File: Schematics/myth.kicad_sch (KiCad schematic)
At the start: 137 parts, among them J1 Conn_01x08_Male, J10 Conn_01x04_Male, J11 Conn_02x01, J2 Conn_01x08_Male, J3 Conn_01x08_Male, J4 Conn_01x08_Male, J5 Conn_01x08_Male, J6 Conn_01x08_Male, J8 Conn_01x08_Male, J9 Conn_01x04_Male, U1 74AHC02, U10 74HC595, U11 74HC165, U12 74AHC08, U13 74HC238, U14 74HC238, U15 74HC238, U16 4002, U17 74HC32, U18 74AHC273, U19 74LS32, U2 74AHC273, U20 CD4532BE, U21 74AHC138, U22 74AHC04, U23 74AHC138, U24 74HC238, U25 74HC238, U26 74LS32, U27 4078, U28 74AHC244, U29 74AHC138, U3 74HC74, U30 74AHC138, U31 4075, U32 74AHC02, U33 74AHC138, U34 74HC238, U35 74AHC138, U36 74HC163, U37 74AHC574, U38 74HC238, U39 74HC32, U4 74AHC04, U40 74AHC04, U41 74AHC574, U42 74HC74, U43 74AHC273, U44 74HC283, U45 74HC283, U46 74AHC273, U47 74HC02, U48 74HC157, U49 74HC157, U5 74AHC04, U50 74AHC244, U51 74AHC04, U52 74HC283, U53 74HC193, U54 74HC193, U55 74HC193, U56 74HC193, U57 74AHC273, U58 74HC193, U59 74HC193, U6 74AHC08, U60 74AHC244, U61 74LS32, U62 4078, U63 74LS08, U64 74LS21, U65 74AHC04, U66 74AHC273, U67 74HC157, U68 74HC157, U7 74HC00, U71 74LS257, U72 74LS257, U73 74HC04, U74 74HC157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

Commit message: Rename G to D as before (D for Data)
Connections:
- net GETG renamed GETD
- net xG renamed xD
- net ~{BOG} renamed ~{BOD}
- net ~{CMacc}: no longer names the net of U47.10, U50.1 (1OE), U50.19 (2OE)
- net ~{COG} renamed ~{COD}
- net ~{GETG} renamed ~{GETD}
- net ~{Gx} renamed ~{Dx}
- net ~{MGacc}: no longer names the net of U47.4, U80.1 (1OE), U80.19 (2OE)
- net ~{MLacc}: no longer names the net of U19.8, U60.1 (1OE), U60.19 (2OE)
- net ~{PUTG} renamed ~{PUTD}
- net ~{opc_GIRO} renamed ~{opc_DIRO}
- net ~{xG} renamed ~{xD}
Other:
- note added: "(DATA) Page Index"
- note added: "D"
- note added: "D/I/R/O"
- note added: "Implementation Semantics: CALL/TRAP: I <= PC, Co <= C, decrement L, PC <= 0, C <= DB0-7 RET: C <= L7, PC <= I, increment L COR: C <= D, PC <= I NEW: L7 <= Co xB does PC-relative in-page branching"
- note removed: "(GLOBAL) Page Index"
- note removed: "G"
- note removed: "G/I/R/O"
- note removed: "Implementation Semantics: CALL/TRAP: I <= PC, Co <= C, decrement L, PC <= 0, C <= DB0-7 RET: C <= L7, PC <= I, increment L COR: C <= G, PC <= I NEW: L7 <= Co xB does a PC-relative in-page branching"
- moved on the sheet: U19C, U32C
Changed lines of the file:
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@@
 	)
 	(junction
+		(at 481.3933 526.1862)
+		(diameter 0)
+		(color 0 0 0 0)
+	)
+	(junction
 		(at 694.4732 536.6399)
 		(diameter 0)
@@
 		)
 	)
+	(wire
+		(pts
+			(xy 484.8212 551.8524) (xy 481.3933 551.8524)
+		)
+		(stroke
+			(width 0)
+			(type default)
+		)
+	)
 	(polyline
 		(pts
@@
 	(wire
 		(pts
-			(xy 533.1407 532.1854) (xy 535.6807 532.1854)
+			(xy 502.6012 554.3924) (xy 500.0612 554.3924)
 		)
 		(stroke
@@
 	(wire
 		(pts
+			(xy 481.3933 551.8524) (xy 481.3933 526.1862)
+		)
+		(stroke
+			(width 0)
+			(type default)
+		)
+	)
+	(wire
+		(pts
 			(xy 1038.9126 182.7303) (xy 1038.9126 221.0698)
 		)
@@
 		)
 	)
-	(text "(GLOBAL)\nPage Index"
+	(text "(DATA)\nPage Index"
 		(exclude_from_sim no)
 		(at 886.2679 522.7559 0)
@@
 		)
 	)
-	(text "G"
+	(text "D"
 		(exclude_from_sim no)
 		(at 870.7275 525.6869 0)
@@
 		)
 	)
-	(text "G/I/R/O"
+	(text "D/I/R/O"
 		(exclude_from_sim no)
 		(at 84.0854 511.9029 0)
@@
 		)
 	)
-	(text "Implementation Semantics:\n\nCALL/TRAP: I <= PC, Co <= C, decrement L, PC <= 0, C <= DB0-7\nRET: C <= L7, PC <= I, increment L\nCOR: C <= G, PC <= I\nNEW: L7 <= Co\n\nxB does a PC-relative in-page branching\n\n"
+	(text "Implementation Semantics:\n\nCALL/TRAP: I <= PC, Co <= C, decrement L, PC <= 0, C <= DB0-7\nRET: C <= L7, PC <= I, increment L\nCOR: C <= D, PC <= I\nNEW: L7 <= Co\n\nxB does PC-relative in-page branching\n\n"
 		(exclude_from_sim no)
 		(at 967.3252 481.683 0)
@@
 	(text "L"
 		(exclude_from_sim no)
-		(at 478.8371 570.0052 0)
+		(at 485.7704 594.8623 0)
 		(effects
 			(font
@@
 	(text "(LOCAL)\nPage index\n(Stack Pointer)"
 		(exclude_from_sim no)
-		(at 494.1251 573.1581 0)
+		(at 501.0584 598.0152 0)
 		(effects
 			(font
@@
 		)
 	)
-	(label "~{CMacc}"
-		(at 694.4732 557.0975 0)
-		(fields_autoplaced yes)
-		(effects
-			(font
-				(size 1.27 1.27)
-			)
-			(justify left bottom)
-		)
-	)
 	(label "FETCH"
 		(at 838.3299 618.4854 180)
@@
 		)
 	)
-	(label "~{GETG}"
+	(label "~{GETD}"
 		(at 746.9641 205.0748 180)
 		(fields_autoplaced yes)
@@
 		)
 	)
-	(label "~{COG}"
+	(label "~{COD}"
 		(at 809.2739 506.3054 180)
 		(fields_autoplaced yes)
@@
 		)
 	)
-	(label "~{MLacc}"
-		(at 550.9207 534.7254 0)
-		(fields_autoplaced yes)
-		(effects
-			(font
-				(size 1.27 1.27)
-			)
-			(justify left bottom)
-		)
-	)
 	(label "PC6"
 		(at 501.9639 208.5014 180)
@@
 		)
 	)
-	(label "~{GETG}"
+	(label "~{GETD}"
 		(at 115.4329 510.5003 0)
 		(fields_autoplaced yes)
@@
 		)
 	)
-	(label "~{opc_GIRO}"
+	(label "~{opc_DIRO}"
 		(at 254.1778 504.1138 0)
 		(fields_autoplaced yes)
@@
 		)
 	)
-	(label "~{BOG}"
+	(label "~{BOD}"
 		(at 834.6739 452.9654 0)
 		(fields_autoplaced yes)
@@
 		)
 	)
-	(label "~{MGacc}"
-		(at 901.9905 417.0084 0)
-		(fields_autoplaced yes)
-		(effects
-			(font
-				(size 1.27 1.27)
-			)
-			(justify left bottom)
-		)
-	)
 	(label "xA"
 		(at 364.9218 304.4698 0)
@@
 		)
 	)
-	(label "GETG"
+	(label "GETD"
 		(at 762.2041 205.0748 0)
 		(fields_autoplaced yes)
@@
 		)
 	)
-	(label "~{Gx}"
+	(label "~{Dx}"
 		(at 362.3818 381.3048 0)
 		(fields_autoplaced yes)
@@
 		)
 	)
-	(label "~{opc_GIRO}"
+	(label "~{opc_DIRO}"
 		(at 67.1729 520.6603 180)
 		(fields_autoplaced yes)
@@
 		)
 	)
-	(label "~{Gx}"
+	(label "~{Dx}"
 		(at 871.5671 479.3249 0)
 		(fields_autoplaced yes)
@@
 		)
 	)
-	(label "~{PUTG}"
+	(label "~{PUTD}"
 		(at 886.8071 481.8649 0)
 		(fields_autoplaced yes)
@@
 		)
 	)
-	(label "~{MLacc}"
-		(at 481.3933 523.6462 180)
-		(fields_autoplaced yes)
-		(effects
-			(font
-				(size 1.27 1.27)
-			)
-			(justify right bottom)
-		)
-	)
 	(label "~{COI}"
 		(at 557.3853 219.1739 180)
@@
 		)
 	)
-	(label "~{COG}"
+	(label "~{COD}"
 		(at 834.6739 447.8854 0)
 		(fields_autoplaced yes)
@@
 		)
 	)
-	(label "~{xG}"
+	(label "~{xD}"
 		(at 706.2737 218.708 180)
 		(fields_autoplaced yes)
@@
 		)
 	)
-	(label "xG"
+	(label "xD"
 		(at 721.5137 218.708 0)
 		(fields_autoplaced yes)
@@
 	)
 	(label "Lx_pre"
-		(at 517.9007 529.6454 180)
+		(at 517.8412 556.9324 0)
 		(fields_autoplaced yes)
 		(effects
@@
 				(size 1.27 1.27)
 			)
-			(justify right bottom)
+			(justify left bottom)
 		)
 	)
@@
 		)
 	)
-	(label "xG"
+	(label "xD"
 		(at 787.454 498.6854 180)
 		(fields_autoplaced yes)
@@
 		)
 	)
-	(label "~{xG}"
+	(label "~{xD}"
 		(at 364.2868 271.4498 0)
 		(fields_autoplaced yes)
@@
 	)
 	(label "GETPUT"
-		(at 535.6807 537.2654 180)
+		(at 500.0612 549.3124 0)
 		(fields_autoplaced yes)
 		(effects
@@
 				(size 1.27 1.27)
 			)
-			(justify right bottom)
+			(justify left bottom)
 		)
 	)
@@
 		)
 	)
-	(label "~{PUTG}"
+	(label "~{PUTD}"
 		(at 115.4329 520.6603 0)
 		(fields_autoplaced yes)
@@
 		)
 	)
-	(label "GETG"
+	(label "GETD"
 		(at 787.454 503.7654 180)
 		(fields_autoplaced yes)
@@
 	)
 	(label "xL_pre"
-		(at 517.9007 534.7254 180)
+		(at 517.8412 551.8524 0)
 		(fields_autoplaced yes)
 		(effects
@@
 				(size 1.27 1.27)
 			)
-			(justify right bottom)
+			(justify left bottom)
 		)
 	)
@@
 		)
 	)
-	(label "~{BOG}"
+	(label "~{BOD}"
 		(at 809.2739 508.8454 180)
 		(fields_autoplaced yes)
@@
 	(symbol
 		(lib_id "74xx:74LS02")
-		(at 525.5207 532.1854 0)
+		(at 510.2212 554.3924 180)
 		(unit 3)
 		(exclude_from_sim no)
@@
 		(dnp no)
 		(property "Reference" "U32"
-			(at 525.5207 523.9304 0)
+			(at 510.2212 562.6474 0)
 			(effects
 				(font
@@
 		)
 		(property "Value" "74AHC02"
-			(at 525.5207 526.2418 0)
+			(at 510.2212 560.336 0)
 			(effects
 				(font
@@
 		)
 		(property "Footprint" "Package_DIP:DIP-14_W7.62mm_Socket_LongPads"
-			(at 525.5207 532.1854 0)
+			(at 510.2212 554.3924 0)
 			(effects
 				(font
@@
 		)
 		(property "Datasheet" "http://www.ti.com/lit/gpn/sn74ls02"
-			(at 525.5207 532.1854 0)
+			(at 510.2212 554.3924 0)
 			(effects
 				(font
@@
 		)
 		(property "Description" ""
-			(at 525.5207 532.1854 0)
+			(at 510.2212 554.3924 0)
 			(effects
 				(font
@@
 	(symbol
 		(lib_id "74xx:74LS32")
-		(at 543.3007 534.7254 0)
+		(at 492.4412 551.8524 180)
 		(unit 3)
 		(exclude_from_sim no)
@@
 		(fields_autoplaced yes)
 		(property "Reference" "U19"
-			(at 543.3007 526.7709 0)
+			(at 492.4412 559.8069 0)
 			(effects
 				(font
@@
 		)
 		(property "Value" "74LS32"
-			(at 543.3007 529.1952 0)
+			(at 492.4412 557.3826 0)
 			(effects
 				(font
@@
 		)
 		(property "Footprint" ""
-			(at 543.3007 534.7254 0)
+			(at 492.4412 551.8524 0)
 			(effects
 				(font
@@
 		)
 		(property "Datasheet" "http://www.ti.com/lit/gpn/sn74LS32"
-			(at 543.3007 534.7254 0)
+			(at 492.4412 551.8524 0)
 			(effects
 				(font
@@
 		)
 		(property "Description" "Quad 2-input OR"
-			(at 543.3007 534.7254 0)
+			(at 492.4412 551.8524 0)
 			(effects
 				(font

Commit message: Relocate pre-built symbol table
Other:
- note added: "NL => NOP (reserved) NM => NOP (reserved) LL => NOP (reserved) LM => NOP (reserved) ML => NOP (reserved) MM => NOP (reserved) DD => NOP (reserved) RR => NOP (reserved) II => NOP (reserved)"
- note added: "Relative Addressing"
- note removed: "NL => NOP (reserved) NM => NOP (reserved) LL => NOP (reserved) LM => NOP (reserved) ML => NOP (reserved) MM => NOP (reserved) GG => NOP (reserved) RR => NOP (reserved) II => NOP (reserved)"
- note removed: "Relative Addressing Unit"
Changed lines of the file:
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@@
 		)
 	)
-	(text "                   NL => NOP (reserved)\n                   NM => NOP (reserved)\n                   LL => NOP (reserved)\n                   LM => NOP (reserved)\n                   ML => NOP (reserved)\n                   MM => NOP (reserved)\n                   GG => NOP (reserved)\n                   RR => NOP (reserved)\n                   II => NOP (reserved)"
+	(text "                   NL => NOP (reserved)\n                   NM => NOP (reserved)\n                   LL => NOP (reserved)\n                   LM => NOP (reserved)\n                   ML => NOP (reserved)\n                   MM => NOP (reserved)\n                   DD => NOP (reserved)\n                   RR => NOP (reserved)\n                   II => NOP (reserved)"
 		(exclude_from_sim no)
 		(at 194.3077 303.7819 0)
 		(effects
 			(font
+				(face "Monaco")
 				(size 1.27 1.27)
 			)
 		)
 	)
-	(text "Relative Addressing Unit"
+	(text "Relative Addressing"
 		(exclude_from_sim no)
-		(at 402.8152 312.0424 0)
+		(at 414.6633 310.4758 0)
 		(effects
 			(font

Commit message: Change mnemonic for NEW to OWN and reorder VM struct
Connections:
- net NEW renamed OWN
- net ~{NEW} renamed ~{OWN}
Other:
- note added: "0 CLR ("Clear" / R:=0) 1 IDO ("Identity O" / R:=O) 2 OCR ("Ones Complement R" / R:=~R) 3 OCO ("Ones Complement O" / R:=~O) 4 SLR ("Shift left R" / R:=R<<1) 5 SLO ("Shift left O" / R:=O<<1) 6 SRR ("Shift right R" / R:=R>>1) 7 SRO ("Shift right O" / R:=O>>1)"
- note added: "Hard wire so that OWN and RET reference L7 ("Owner")"
- note added: "Implementation Semantics: CALL/TRAP: I <= PC, Co <= C, decrement L, PC <= 0, C <= DB0-7 RET: C <= L7, PC <= I, increment L COR: C <= D, PC <= I OWN: L7 <= Co xB does PC-relative in-page branching"
- note removed: "0 CLR ("Clear" / R:=0) 1 IDO ("Identity O" / R:=Old) 2 OCR ("Ones Complement R" / R:=~R) 3 OCO ("Ones Complement O" / R:=~O) 4 SLR ("Shift left New" / R:=R<<1) 5 SLO ("Shift left Old" / R:=O<<1) 6 SRR ("Shift right R" / R:=R>>1) 7 SRO ("Shift right O" / R:=O>>1)"
- note removed: "Force ENTER/LEAVE/FAR ref L7 ("Owner")"
- note removed: "Implementation Semantics: CALL/TRAP: I <= PC, Co <= C, decrement L, PC <= 0, C <= DB0-7 RET: C <= L7, PC <= I, increment L COR: C <= D, PC <= I NEW: L7 <= Co xB does PC-relative in-page branching"
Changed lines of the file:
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@@
 	(title_block
 		(title "Sonne-8 Micro-Controller")
-		(date "2024-09-05")
+		(date "2024-09-07")
 		(rev "Myth")
 		(company "Contact: mim@ok-schalter.de")
@@
 		)
 	)
-	(text "0 CLR (\"Clear\" / R:=0)\n1 IDO (\"Identity O\" / R:=Old)\n2 OCR (\"Ones Complement R\" / R:=~R)\n3 OCO (\"Ones Complement O\" / R:=~O)\n4 SLR (\"Shift left New\" / R:=R<<1)\n5 SLO (\"Shift left Old\" / R:=O<<1)\n6 SRR (\"Shift right R\" / R:=R>>1)\n7 SRO (\"Shift right O\" / R:=O>>1)"
+	(text "0 CLR (\"Clear\" / R:=0)\n1 IDO (\"Identity O\" / R:=O)\n2 OCR (\"Ones Complement R\" / R:=~R)\n3 OCO (\"Ones Complement O\" / R:=~O)\n4 SLR (\"Shift left R\" / R:=R<<1)\n5 SLO (\"Shift left O\" / R:=O<<1)\n6 SRR (\"Shift right R\" / R:=R>>1)\n7 SRO (\"Shift right O\" / R:=O>>1)"
 		(exclude_from_sim no)
 		(at 1080.1979 391.3049 0)
@@
 		)
 	)
-	(text "Implementation Semantics:\n\nCALL/TRAP: I <= PC, Co <= C, decrement L, PC <= 0, C <= DB0-7\nRET: C <= L7, PC <= I, increment L\nCOR: C <= D, PC <= I\nNEW: L7 <= Co\n\nxB does PC-relative in-page branching\n\n"
+	(text "Implementation Semantics:\n\nCALL/TRAP: I <= PC, Co <= C, decrement L, PC <= 0, C <= DB0-7\nRET: C <= L7, PC <= I, increment L\nCOR: C <= D, PC <= I\nOWN: L7 <= Co\n\nxB does PC-relative in-page branching\n\n"
 		(exclude_from_sim no)
 		(at 967.3252 481.683 0)
@@
 		)
 	)
-	(text "Force ENTER/LEAVE/FAR\nref L7 (\"Owner\")"
+	(text "Hard wire so that OWN and RET \nreference L7 (\"Owner\")"
 		(exclude_from_sim no)
-		(at 889.9284 579.7445 0)
+		(at 876.1322 582.1109 0)
 		(effects
 			(font
@@
 		)
 	)
-	(label "~{NEW}"
+	(label "~{OWN}"
 		(at 749.6363 161.9153 180)
 		(fields_autoplaced yes)
@@
 		)
 	)
-	(label "~{NEW}"
+	(label "~{OWN}"
 		(at 671.6372 613.8228 180)
 		(fields_autoplaced yes)
@@
 		)
 	)
-	(label "NEW"
+	(label "OWN"
 		(at 764.8763 161.9153 0)
 		(fields_autoplaced yes)
@@
 		)
 	)
-	(label "NEW"
+	(label "OWN"
 		(at 941.5443 579.3538 180)
 		(fields_autoplaced yes)
@@
 		)
 	)
-	(label "~{NEW}"
+	(label "~{OWN}"
 		(at 216.6174 392.7348 0)
 		(fields_autoplaced yes)
@@
 		)
 	)
-	(label "NEW"
+	(label "OWN"
 		(at 812.4552 675.102 180)
 		(fields_autoplaced yes)
@@
 		)
 	)
-	(label "~{NEW}"
+	(label "~{OWN}"
 		(at 1117.9585 624.302 0)
 		(fields_autoplaced yes)

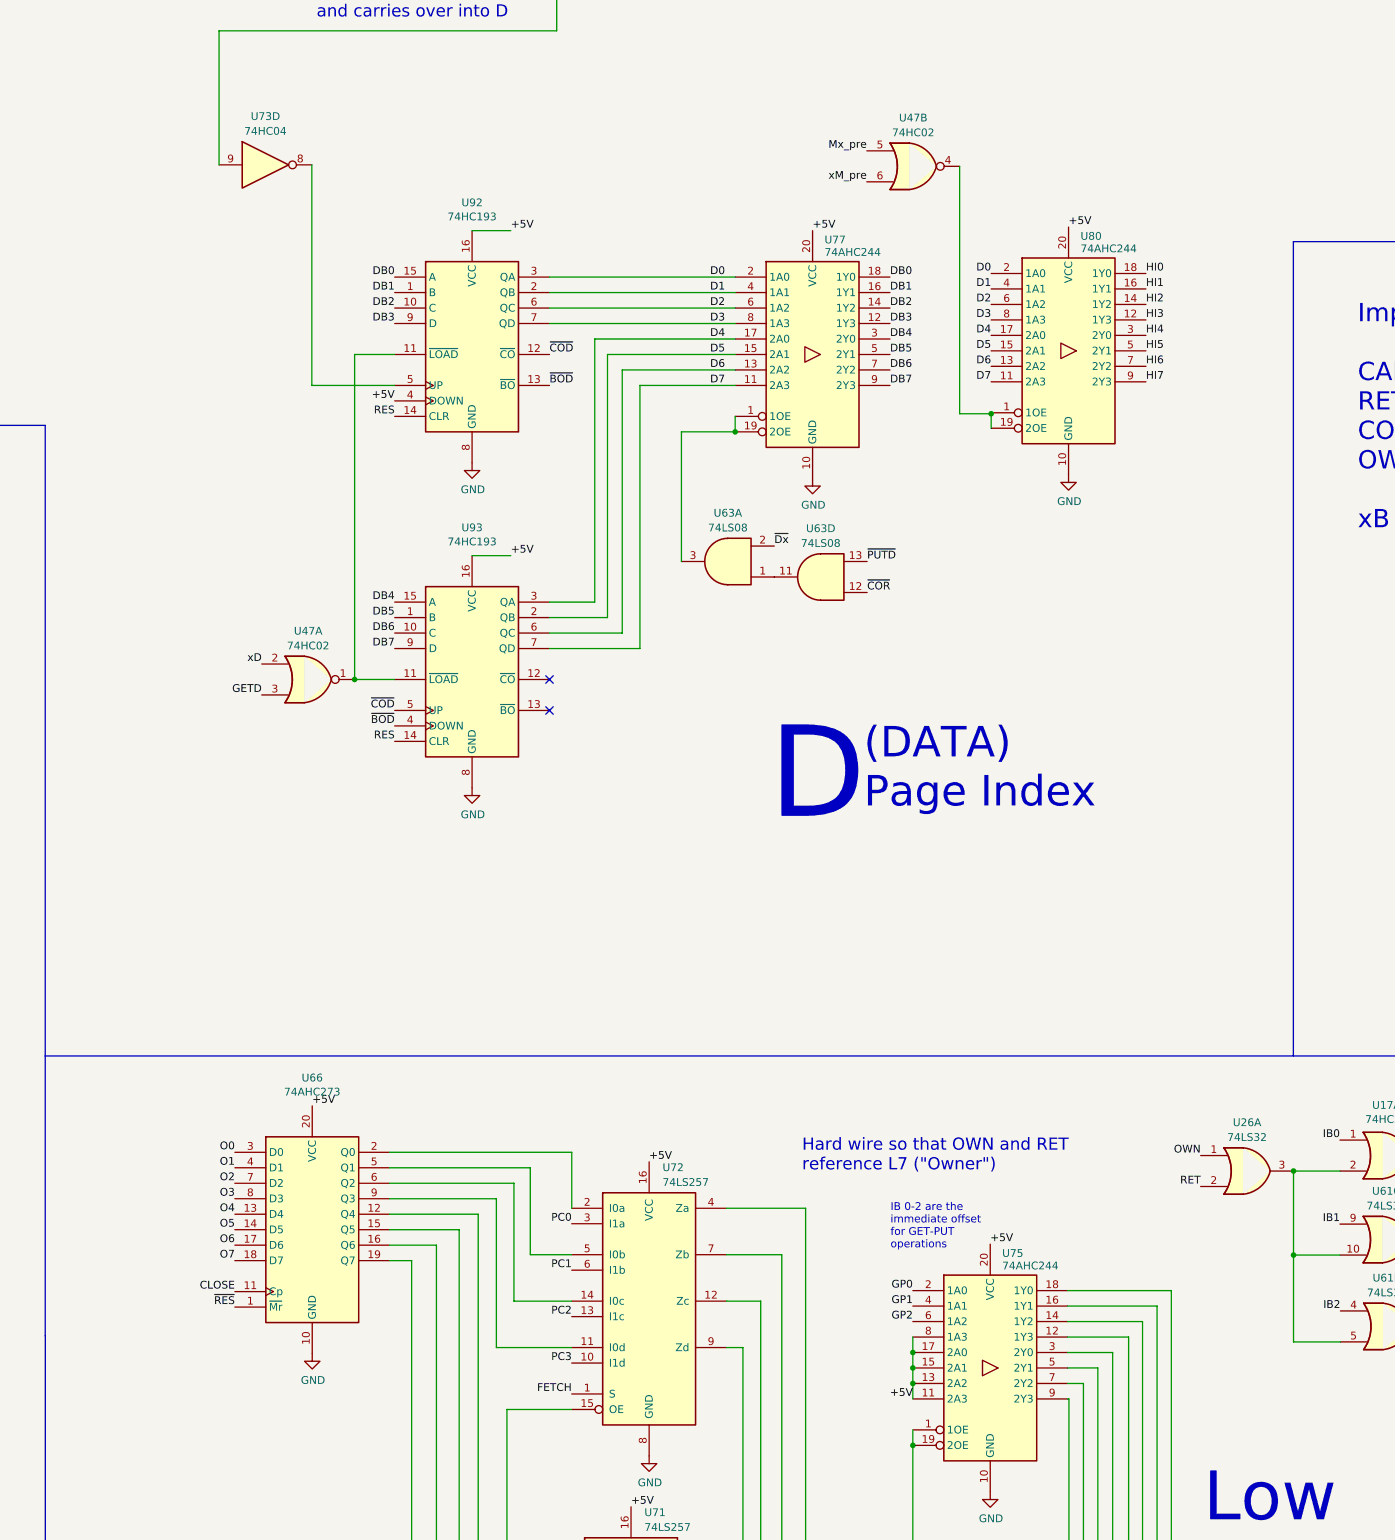
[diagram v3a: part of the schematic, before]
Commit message: Create JSON file with info on each instruction
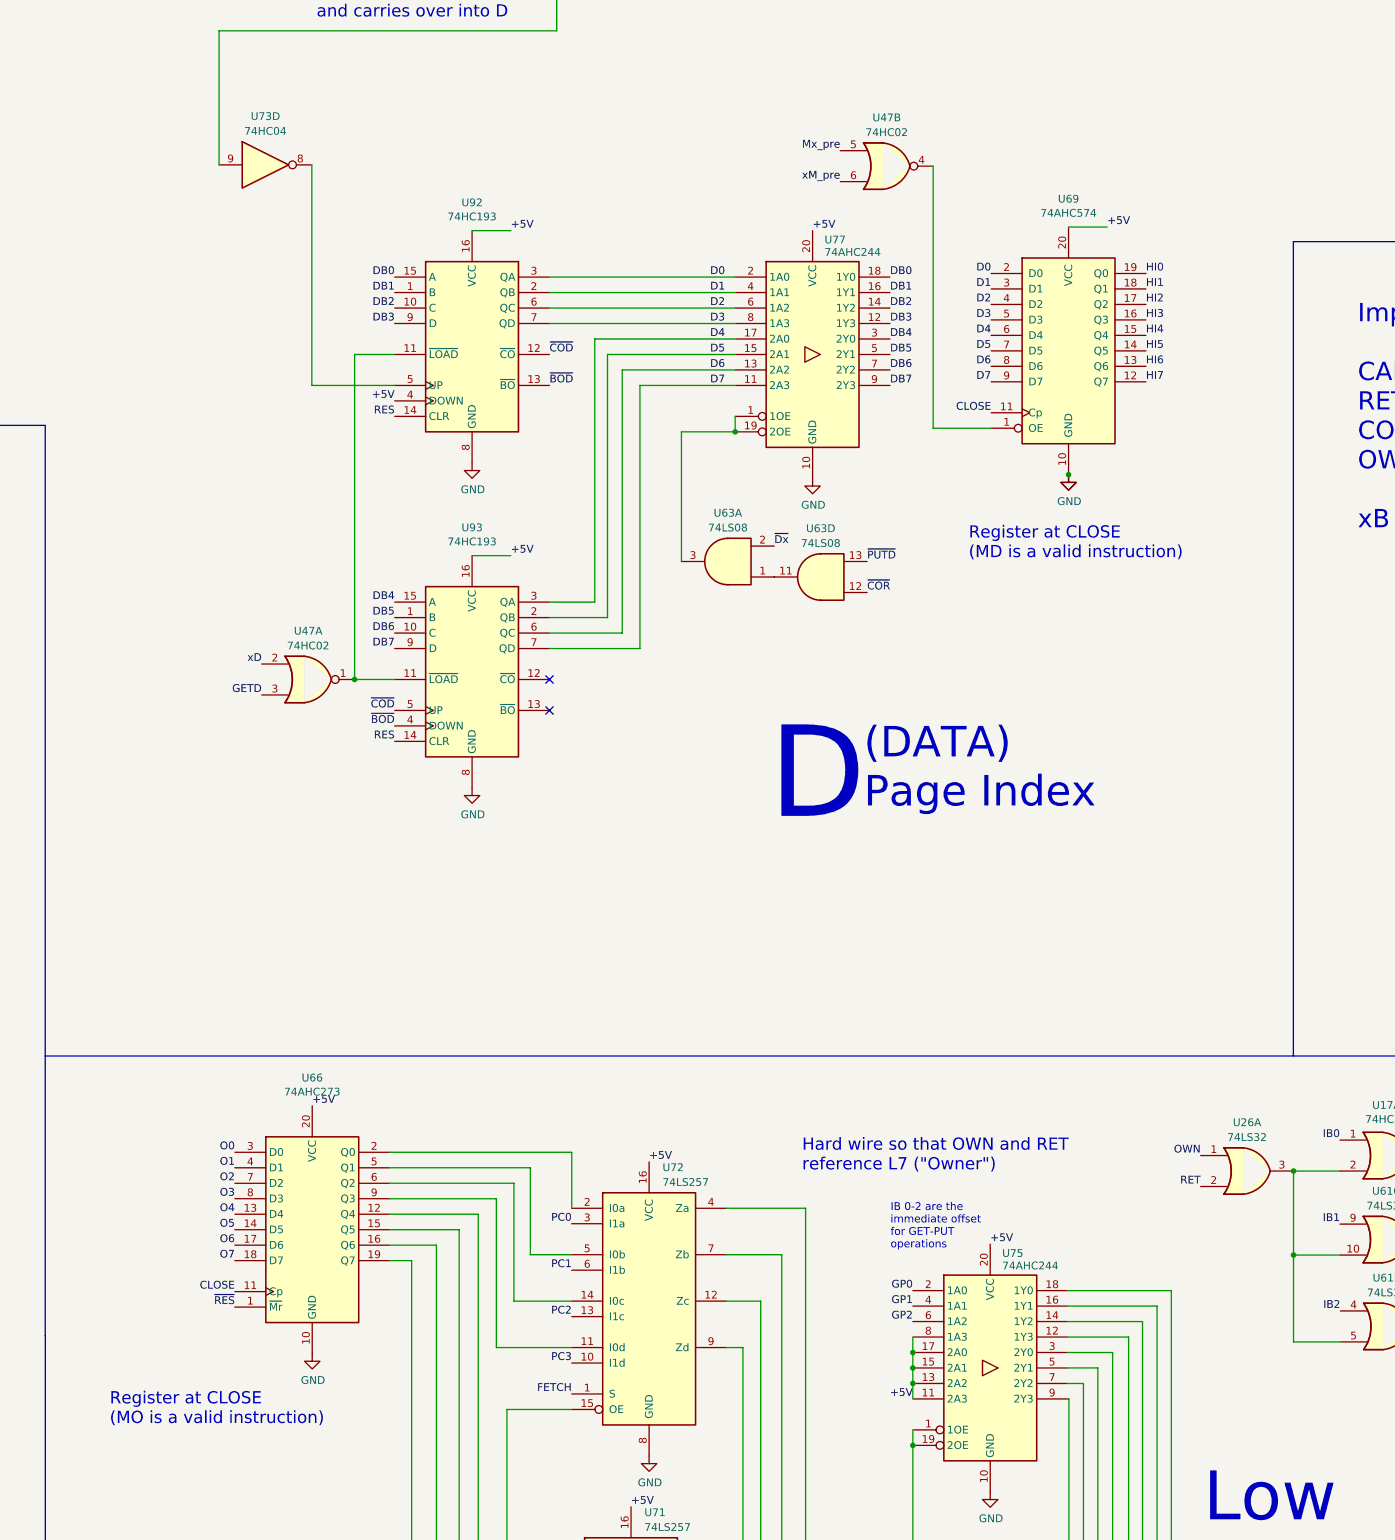
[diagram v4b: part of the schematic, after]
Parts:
- removed U80: 74AHC244, Package_DIP:DIP-20_W7.62mm_Socket_LongPads, symbol 74xx:74AHC244
- added U69: 74AHC574, Package_DIP:DIP-20_W7.62mm_Socket_LongPads, symbol 74xx:74LS574
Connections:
- net +5V: now also U69.20 (VCC)
- net CLOSE: now also U69.11 (Cp)
- net D0: now also U69.2 (D0)
- net D1: now also U69.3 (D1)
- net D2: now also U69.4 (D2)
- net D3: now also U69.5 (D3)
- net D4: now also U69.6 (D4)
- net D5: now also U69.7 (D5)
- net D6: now also U69.8 (D6)
- net D7: now also U69.9 (D7)
- net GND: now also U69.10 (GND)
- net HI0: now also U69.19 (Q0)
- net HI1: now also U69.18 (Q1)
- net HI2: now also U69.17 (Q2)
- net HI3: now also U69.16 (Q3)
- net HI4: now also U69.15 (Q4)
- net HI5: now also U69.14 (Q5)
- net HI6: now also U69.13 (Q6)
- net HI7: now also U69.12 (Q7)
- net at U47.4: now also U69.1 (OE)
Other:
- note added: "Register at CLOSE (MD is a valid instruction)"
- note added: "Register at CLOSE (MO is a valid instruction)"
- moved on the sheet: U47B
